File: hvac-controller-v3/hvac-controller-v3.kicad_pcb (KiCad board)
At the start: 2 copper layers, 50 x 30 mm, 48 parts, among them J1 VAC IN, J2 Conn_01x06, J3 UART, U1 ESP32-C3-MINI-1, U2 LM324DT, U3 TPS5430DDA, U4 TPS5430DDA

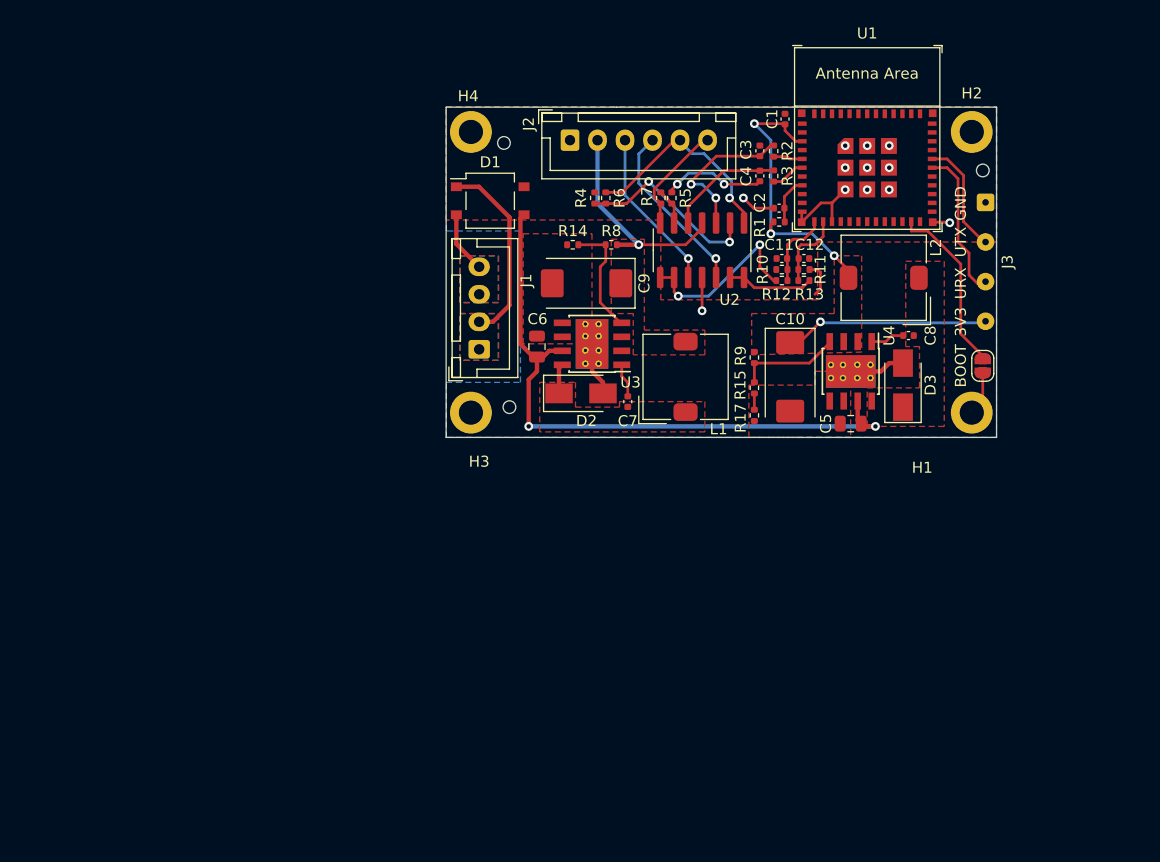
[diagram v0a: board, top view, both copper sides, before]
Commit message: Add v2.1 and v3
To try to make it smaller
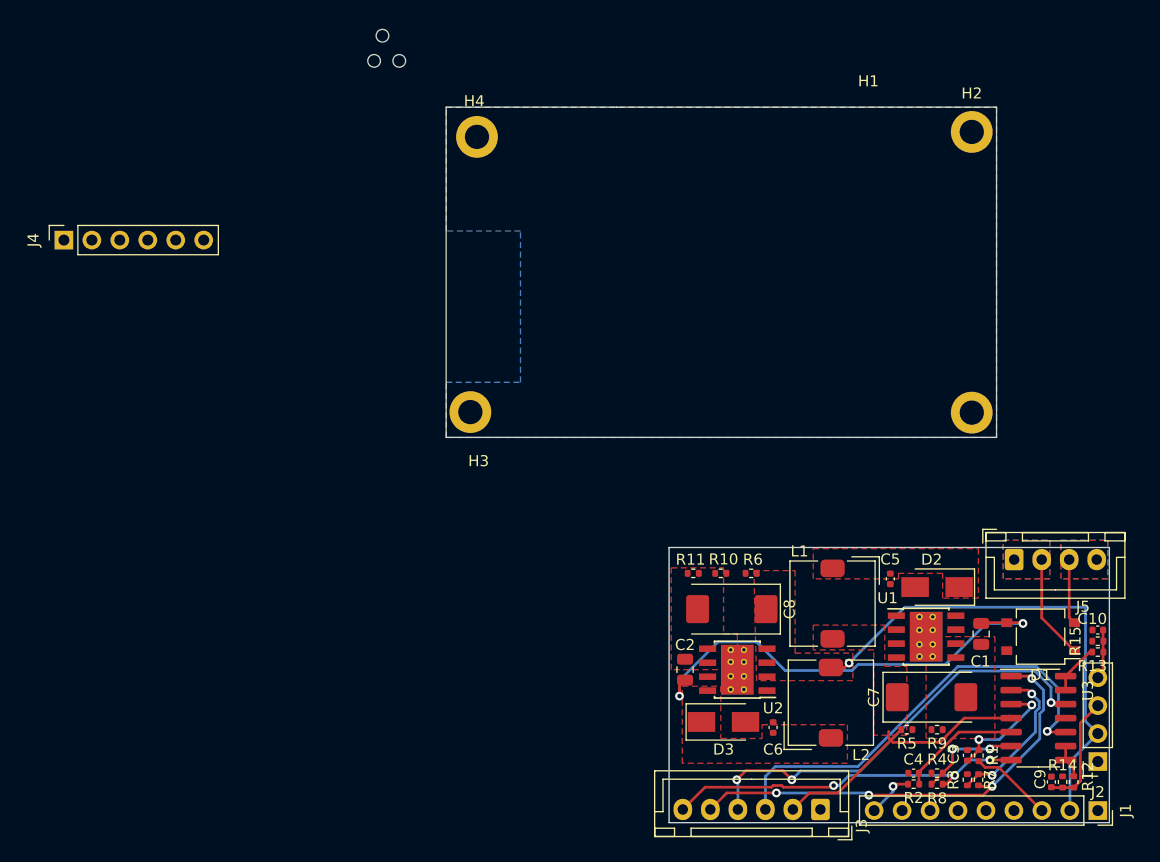
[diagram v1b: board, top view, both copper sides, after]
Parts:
- removed the C1 at (113.8, 87.6)
- removed the C2 at (113.2, 95.7)
- removed the J3 at (132.0, 95.2)
- removed JP1: BOOT, Jumper:SolderJumper-2_P1.3mm_Open_RoundedPad1.0x1.5mm
- removed the R1 at (113.2, 96.9)
- removed the U1 at (121.2, 92.0)
- added J1: Conn_M5Stamp_Pico_01x09_Female, Connector_PinSocket_2.54mm:PinSocket_1x09_P2.54mm_Vertical, F.Cu at (142.2, 150.4)
- added J2: Conn_M5Stamp_Pico_01x04_Female, Connector_PinSocket_2.54mm:PinSocket_1x04_P2.54mm_Vertical, F.Cu at (142.2, 145.9)
- added J4: Conn_M5Stamp_Pico_01x06_Female, Connector_PinSocket_2.54mm:PinSocket_1x06_P2.54mm_Vertical, F.Cu at (48.3, 98.6)
- moved J3 64.9 mm to (117.0, 150.3), turned to 180 degrees
- moved D1 63.8 mm to (137.0, 134.6), turned to 180 degrees
- moved R7 62.8 mm to (131.4, 147.6), turned to -90 degrees
- moved R3 62.8 mm to (130.3, 147.6)
- moved R8 58.9 mm to (127.6, 148.0), turned to 0 degrees
- moved C3 58.1 mm to (130.3, 145.4)
- moved R1 58.0 mm to (131.4, 145.4)
- moved R4 57.5 mm to (127.6, 147.0), turned to 180 degrees
- moved R2 56.7 mm to (125.5, 148.0), turned to 180 degrees
- moved C4 56.0 mm to (125.5, 147.0), turned to 180 degrees
- moved H6 55.9 mm to (77.2, 80.0)
- moved R9 55.1 mm to (127.6, 143.1), turned to 180 degrees
- moved C9 53.5 mm to (138.0, 147.8), turned to -90 degrees
- moved R14 53.1 mm to (139.0, 147.8), turned to 90 degrees
- moved R12 52.7 mm to (140.0, 147.8), turned to -90 degrees
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- renumbered C6 to C1, C12 to C10, C5 to C2, C7 to C5, C8 to C6, C9 to C7, C10 to C8, C11 to C9, J2 to J3, J1 to J5, R2 to R1, R15 to R10, R17 to R11, R10 to R12, R11 to R13, R12 to R14, R13 to R15, R3 to R2, R4 to R3, R5 to R4, R8 to R5, R9 to R6, R6 to R7, R7 to R8, R14 to R9, U3 to U1, U4 to U2, U2 to U3
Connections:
- net +3V3 renamed +5V
- R1 pad 2: /PWM1 -> /DAC1
- R2 pad 2: /PWM2 -> /DAC2
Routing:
- net GND: track 40.9 -> 0.00 mm, vias 14 -> 0
- net /CTRL1_IN: track 14.9 -> 40.6 mm
- net /CTRL2_IN: track 16.0 -> 39.5 mm, vias 1 -> 3
- net /CTRL2_OUT: track 10.0 -> 33.2 mm, vias 0 -> 3
- net /CTRL1_OUT: track 19.6 -> 42.0 mm, vias 1 -> 4
- net Net-(JP1-Pad1): track 16.1 -> 0.00 mm
- net Net-(C1-Pad1): track 58.1 -> 42.4 mm
- net /UART_RX: track 13.7 -> 0.00 mm
- net Net-(R12-Pad1): track 16.5 -> 3.06 mm, vias 2 -> 0
- net Net-(R5-Pad2): track 10.7 -> 0.00 mm
- net /UART_TX: track 10.5 -> 0.00 mm
- net Net-(R10-Pad2): track 9.45 -> 0.00 mm
- net -24VA: track 17.3 -> 9.50 mm
- net /DAC1: track 0.00 -> 7.58 mm
- net Net-(R4-Pad1): track 3.29 -> 9.44 mm, vias 0 -> 2
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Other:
- board size 50 x 30 mm -> 60.2 x 65 mm
- board text removed: "3V3"
- board text removed: "URX"
- board text removed: "UTX"
